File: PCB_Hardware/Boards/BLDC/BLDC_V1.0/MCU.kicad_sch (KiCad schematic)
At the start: 15 parts, among them J7 Conn_ARM_SWD_TagConnect_TC2030, U7 STM32G474RET6, Y2 XXGBBCNANF-25.000000MHZ

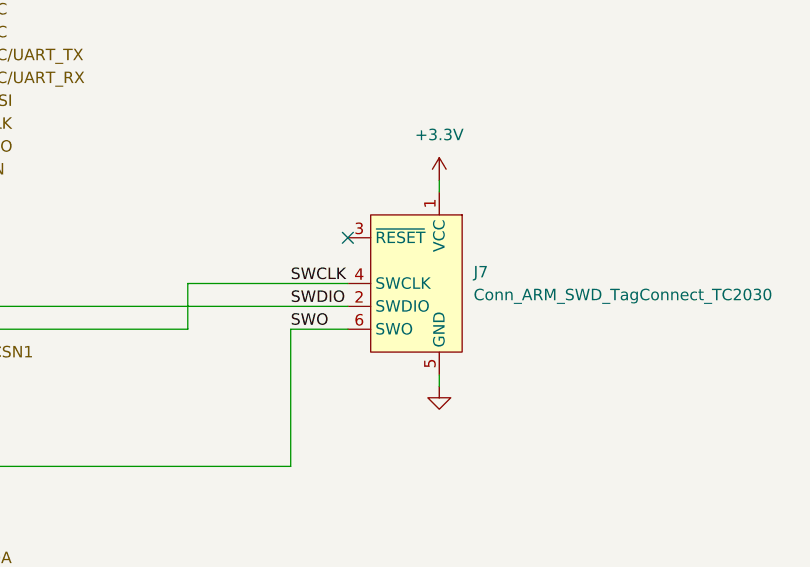
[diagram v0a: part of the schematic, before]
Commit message: minor BLDC changes and production files for ordering
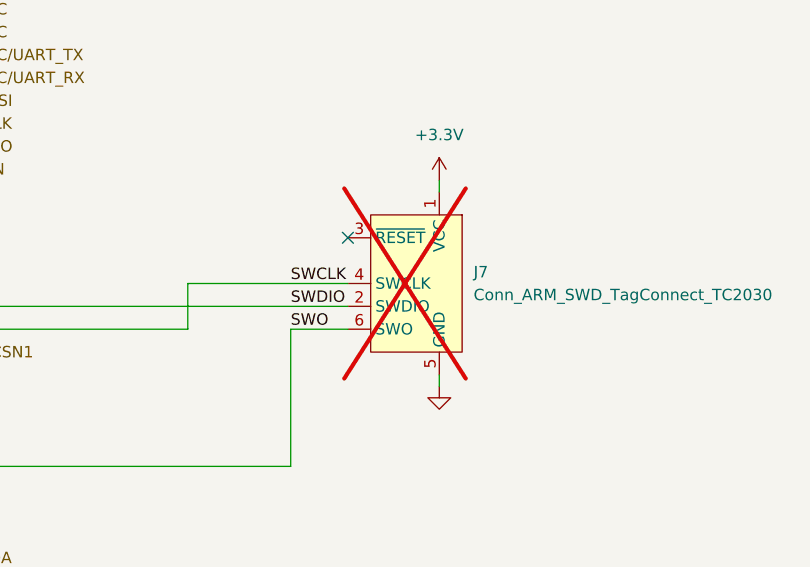
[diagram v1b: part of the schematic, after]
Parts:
- C30: Manufacturer_Part_Number (none) -> CL10A475MQ8NNNC
- C31, C32, C33, C34, C35, C36, C42, C45: Manufacturer_Part_Number (none) -> CC0402ZRY5V6BB104; Price (none) -> 0.0015
- C43, C44: Manufacturer_Part_Number (none) -> CC0402JRNPO8BN180
- J7: now not fitted
- R24: Manufacturer_Part_Number (none) -> RC0402JR-130RL
- U7: Manufacturer_Part_Number (none) -> STM32G474RET6
- Y2: Manufacturer_Part_Number (none) -> XXGBBCNANF-25.000000MHZ
